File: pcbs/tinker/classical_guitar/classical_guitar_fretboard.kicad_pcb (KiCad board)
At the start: 4 copper layers, 188 parts, among them Q1 AO3401A, U1 AT42QT1110-A, U2 AT42QT1110-A, U3 AT42QT1110-A, U4 MP2359

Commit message: Prepare electrode tracking
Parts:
- removed Udecoder4_to_161: CD74HC154ME4, Package_SO:SOIC-24W_7.5x15.4mm_P1.27mm
- added Dec1: CD74HC4515M, Package_SO:SOIC-24W_7.5x15.4mm_P1.27mm, F.Cu at (43.2, 112.2)
- Jdecoder4_to_16_input1: value Conn_01x04_Male -> Conn_01x06_Male; footprint Connector_PinSocket_2.54mm:PinSocket_1x04_P2.54mm_Vertical -> Connector_PinHeader_2.54mm:PinHeader_1x06_P2.54mm_Vertical
- moved Jcommon_spi1 54.4 mm to (65.6, 81.1)
- moved Jdecoder4_to_16_output1 51.9 mm to (58.4, 131.3), turned to 180 degrees
- moved Jdecoder4_to_16_input1 49.5 mm to (30.5, 119.0), turned to 180 degrees
- moved Jch1 19.8 mm to (65.6, 69.8)
- moved Jsync1 19.8 mm to (65.6, 63.6)
- moved Rch1 19.8 mm to (58.8, 63.4)
- moved JPch1 19.8 mm to (60.0, 68.4)
- moved JPch2 19.8 mm to (60.0, 72.4)
- moved JPch3 19.8 mm to (60.0, 76.4)
- moved D1 6.27 mm to (58.8, 23.2)
- moved Jpower1 5.22 mm to (30.5, 38.1)
- moved Q1 3.71 mm to (54.0, 28.1)
- moved F1 3.48 mm to (60.6, 30.8)
- moved D2 0.40 mm to (53.2, 38.0)
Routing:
- net Net-(Dec1-Pad1): track 35.9 -> 7.69 mm
- net Net-(Dec1-Pad21): track 0.00 -> 21.7 mm
- net Net-(Dec1-Pad23): track 34.4 -> 13.5 mm
- net Net-(Dec1-Pad15): track 41.3 -> 23.0 mm
- net Net-(Dec1-Pad13): track 31.6 -> 14.8 mm
- net Net-(Dec1-Pad5): track 6.80 -> 22.5 mm
- net Net-(Dec1-Pad4): track 7.33 -> 23.0 mm
- net Net-(Dec1-Pad6): track 6.78 -> 22.4 mm
- net Net-(Dec1-Pad7): track 7.31 -> 22.4 mm
- net Net-(Dec1-Pad8): track 8.26 -> 21.9 mm
- net Net-(Dec1-Pad9): track 9.94 -> 23.5 mm, vias 0 -> 2
- net Net-(Dec1-Pad16): track 36.4 -> 23.4 mm, vias 0 -> 2
- net GND: track 0.00 -> 12.7 mm
- net VDD: track 0.00 -> 12.5 mm
- net /mp2359/BUCK_SW: track 0.00 -> 11.9 mm
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
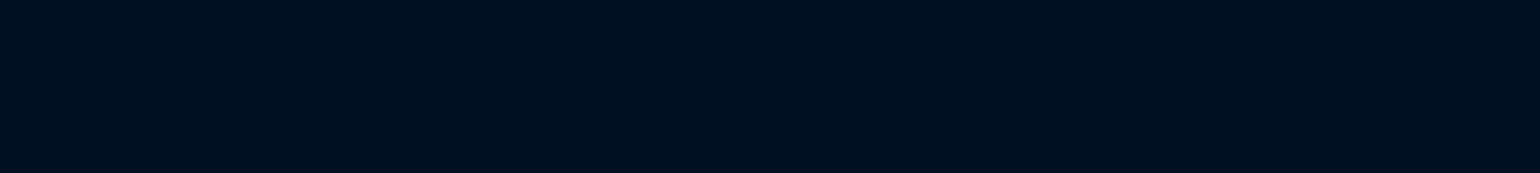
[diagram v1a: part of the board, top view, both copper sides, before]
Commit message: Adjusted last_move
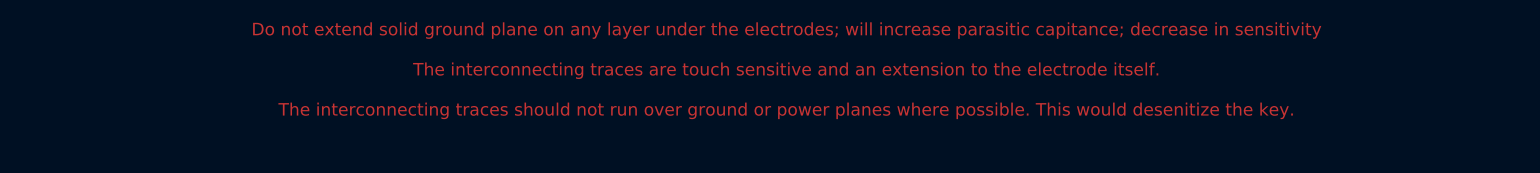
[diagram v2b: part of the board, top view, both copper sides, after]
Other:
- board text added: "Do not extend solid ground plane on any layer under the electrodes; will increase parasitic capitance; decrease in sensitivity The interconnecting traces are touch sensitive and an extension to the electrode itself. The interconnecting traces should not run over ground or power planes where possible. This would desenitize the key."
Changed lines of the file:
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@@
   (general
     (thickness 1.6)
-    (drawings 0)
+    (drawings 1)
     (tracks 742)
     (zones 0)
@@
     )
   )
+  (gr_text "Do not extend solid ground plane on any layer under the electrodes; will increase parasitic capitance; decrease in sensitivity\n\nThe interconnecting traces are touch sensitive and an extension to the electrode itself. \n\nThe interconnecting traces should not run over ground or power planes where possible. This would desenitize the key." (at 172.325 -24.35) (layer F.Cu)
+    (effects (font (size 1.5 1.5) (thickness 0.3)))
+  )
   (segment (start 85.6175 28.125) (end 85.525 28.0325) (width 0.3) (layer F.Cu) (net 1))

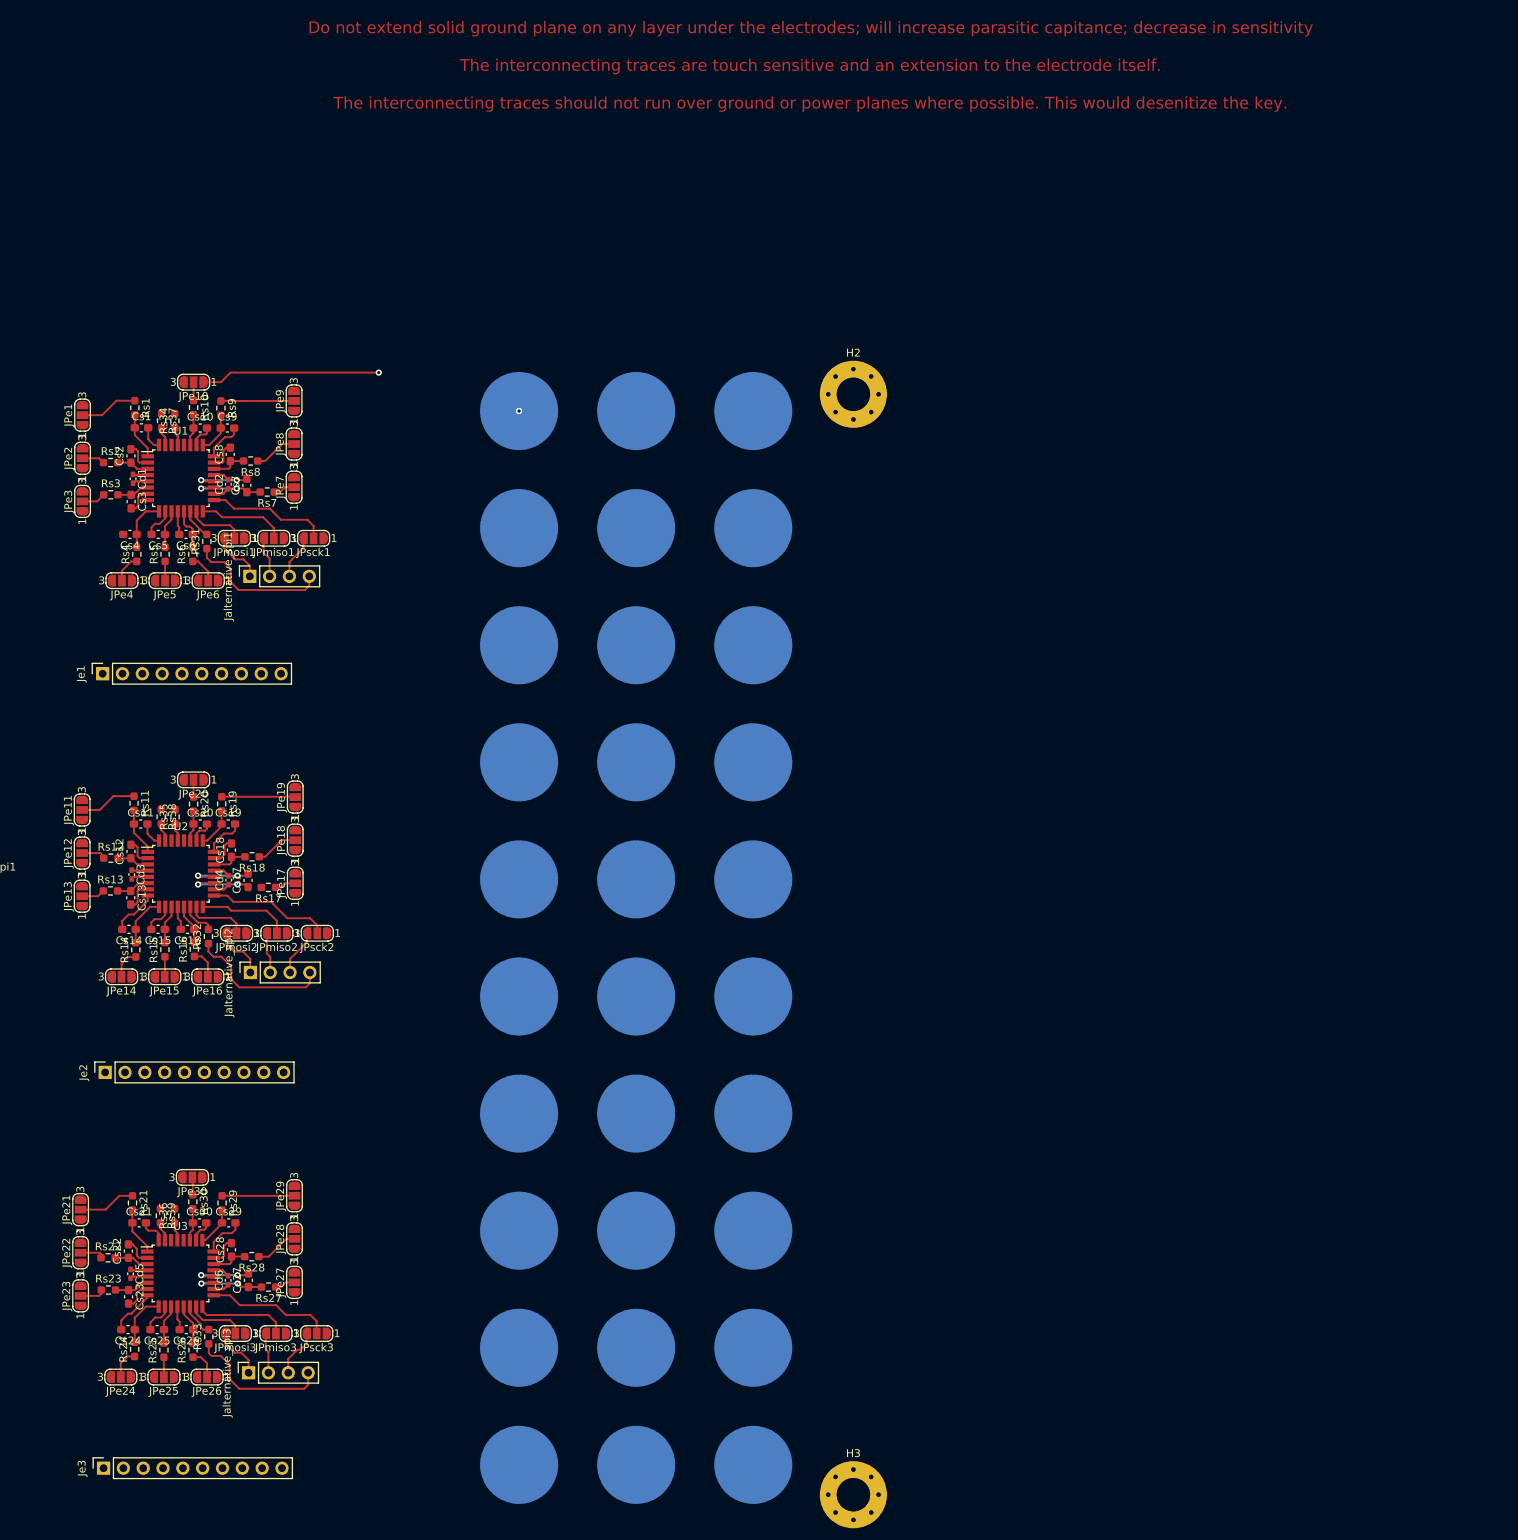
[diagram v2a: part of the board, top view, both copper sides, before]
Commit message: Tracing electrodes
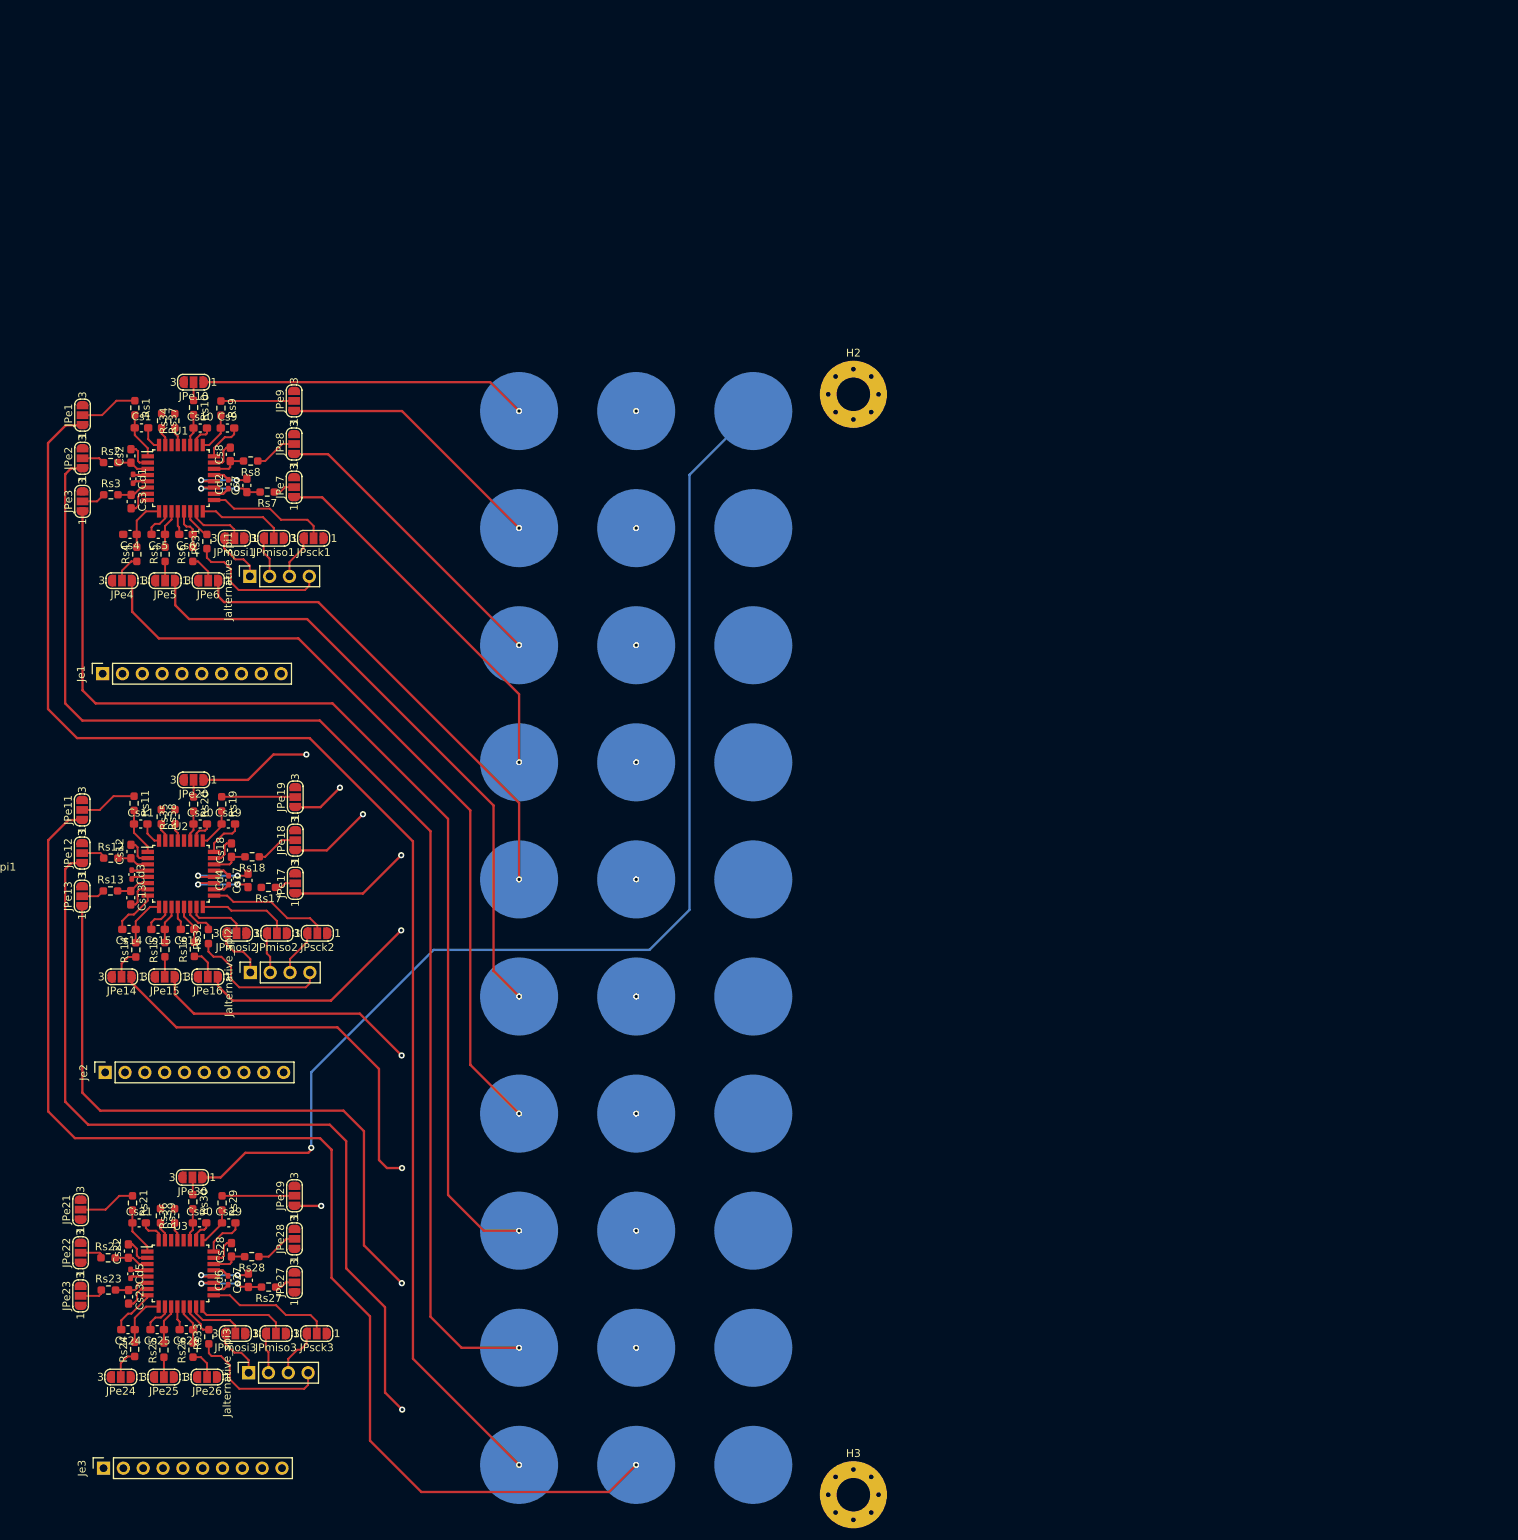
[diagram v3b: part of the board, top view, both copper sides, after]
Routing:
- net Net-(E1-Pad1): track 0.00 -> 178.7 mm, vias 0 -> 1
- net Net-(E2-Pad1): track 0.00 -> 160.7 mm, vias 0 -> 1
- net Net-(E11-Pad1): track 0.00 -> 156.1 mm, vias 0 -> 1
- net Net-(E30-Pad1): track 0.00 -> 149.7 mm, vias 0 -> 1
- net Net-(E12-Pad1): track 0.00 -> 141.0 mm, vias 0 -> 2
- net Net-(E3-Pad1): track 0.00 -> 135.7 mm, vias 0 -> 1
- net Net-(E13-Pad1): track 0.00 -> 116.3 mm, vias 0 -> 2
- net Net-(E4-Pad1): track 0.00 -> 99.3 mm, vias 0 -> 1
- net Net-(E14-Pad1): track 0.00 -> 84.9 mm, vias 0 -> 2
- net Net-(E20-Pad1): track 0.00 -> 82.1 mm, vias 0 -> 2
- net Net-(E5-Pad1): track 0.00 -> 80.4 mm, vias 0 -> 1
- net Net-(E15-Pad1): track 0.00 -> 67.7 mm, vias 0 -> 2
- net Net-(E16-Pad1): track 0.00 -> 62.0 mm, vias 0 -> 2
- net Net-(E6-Pad1): track 0.00 -> 61.3 mm, vias 0 -> 1
- net Net-(E19-Pad1): track 0.00 -> 58.9 mm, vias 0 -> 2
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
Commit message: Traced electrodes
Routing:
- net Net-(E29-Pad1): track 3.42 -> 152.4 mm, vias 1 -> 4
- net Net-(E21-Pad1): track 0.00 -> 130.9 mm, vias 0 -> 1
- net Net-(E28-Pad1): track 0.00 -> 130.2 mm, vias 0 -> 3
- net Net-(E22-Pad1): track 0.00 -> 129.7 mm, vias 0 -> 4
- net Net-(E26-Pad1): track 0.00 -> 127.0 mm, vias 0 -> 3
- net Net-(E27-Pad1): track 0.00 -> 125.2 mm, vias 0 -> 3
- net Net-(E23-Pad1): track 0.00 -> 121.8 mm, vias 0 -> 3
- net Net-(E25-Pad1): track 0.00 -> 120.0 mm, vias 0 -> 5
- net Net-(E24-Pad1): track 0.00 -> 118.4 mm, vias 0 -> 3
- net Net-(E30-Pad1): track 149.7 -> 165.7 mm, vias 1 -> 2
- net Net-(E1-Pad1): track 178.7 -> 185.2 mm
- net Net-(E11-Pad1): track 156.1 -> 157.8 mm

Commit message: Traced 1st at42qt1110
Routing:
- net Net-(Jsync1-Pad1): track 0.00 -> 168.4 mm, vias 0 -> 2
- net /C_MISO: track 0.00 -> 119.0 mm, vias 0 -> 6
- net /C_SCK: track 0.00 -> 115.7 mm, vias 0 -> 4
- net /C_MOSI: track 0.00 -> 102.5 mm, vias 0 -> 4
- net /Change1: track 0.00 -> 85.1 mm
- net Net-(JPe10-Pad3): track 0.00 -> 77.3 mm, vias 0 -> 12
- net /Change3: track 0.00 -> 68.8 mm
- net Net-(JPe9-Pad3): track 0.00 -> 62.6 mm, vias 0 -> 8
- net /Change2: track 0.00 -> 58.5 mm, vias 0 -> 6
- net Net-(JPe8-Pad3): track 0.00 -> 47.2 mm, vias 0 -> 6
- net Net-(JPe1-Pad3): track 0.00 -> 43.0 mm, vias 0 -> 3
- net Net-(JPe7-Pad3): track 0.00 -> 40.3 mm, vias 0 -> 4
- net Net-(JPe2-Pad3): track 0.00 -> 33.5 mm, vias 0 -> 2
- net Net-(JPe3-Pad3): track 0.00 -> 33.2 mm, vias 0 -> 2
- net Net-(JPe4-Pad3): track 0.00 -> 14.6 mm
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
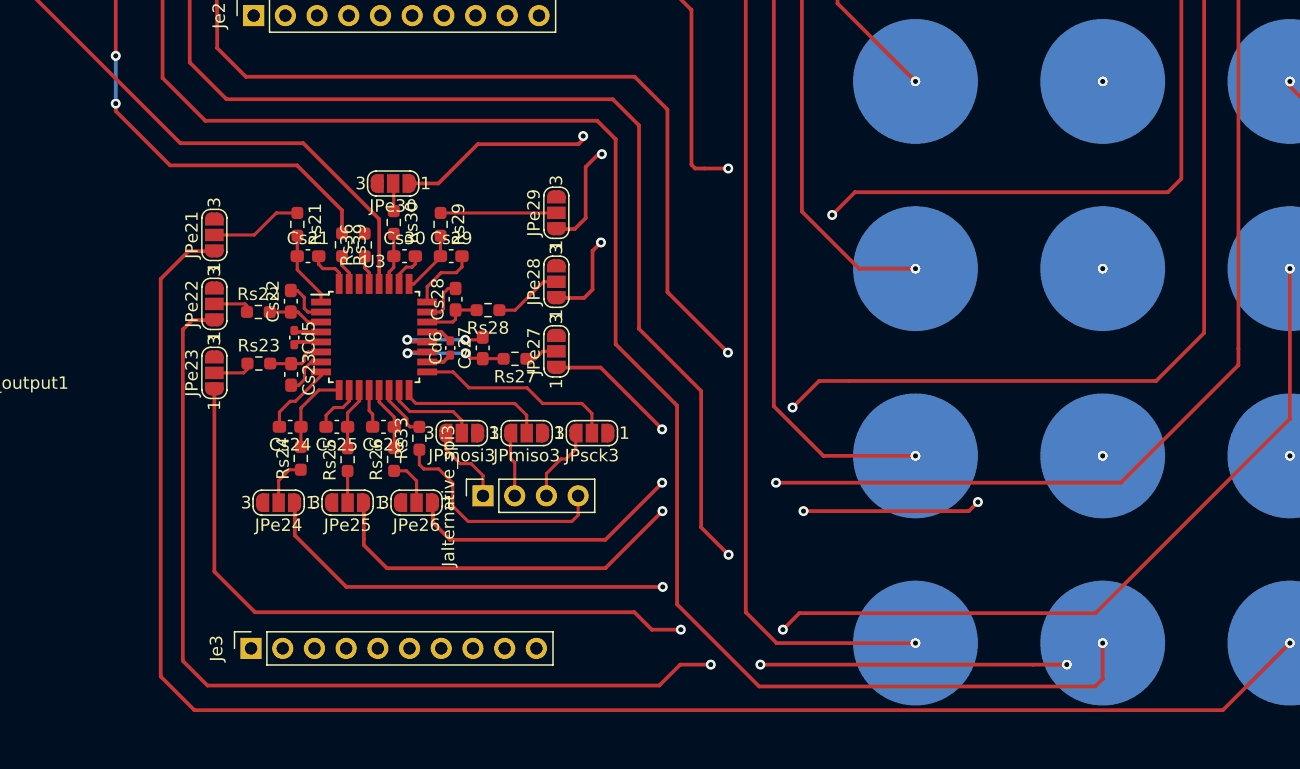
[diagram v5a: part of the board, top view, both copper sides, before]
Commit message: Traced 2nd at42qt1110
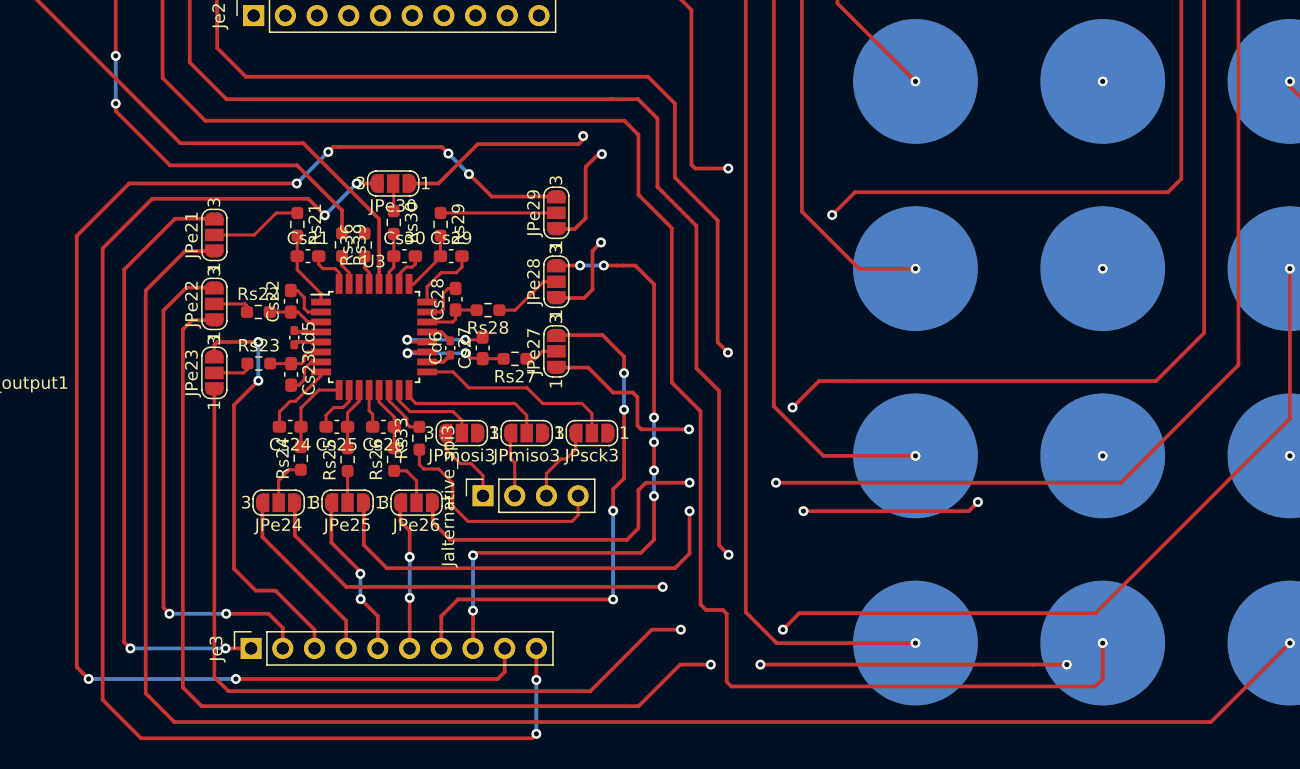
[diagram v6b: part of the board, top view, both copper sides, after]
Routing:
- net Net-(JPe29-Pad3): track 0.00 -> 114.4 mm, vias 0 -> 6
- net Net-(JPe30-Pad3): track 0.00 -> 104.4 mm, vias 0 -> 4
- net Net-(JPe28-Pad3): track 0.00 -> 51.4 mm, vias 0 -> 8
- net Net-(JPe21-Pad3): track 0.00 -> 49.1 mm, vias 0 -> 2
- net Net-(JPe27-Pad3): track 0.00 -> 42.9 mm, vias 0 -> 4
- net Net-(JPe22-Pad3): track 0.00 -> 40.5 mm, vias 0 -> 2
- net Net-(JPe23-Pad3): track 0.00 -> 33.5 mm, vias 0 -> 2
- net Net-(JPe24-Pad3): track 0.00 -> 14.5 mm
- net Net-(JPe25-Pad3): track 0.00 -> 13.2 mm, vias 0 -> 2
- net Net-(JPe26-Pad3): track 0.00 -> 12.0 mm, vias 0 -> 2
- net Net-(E23-Pad1): track 121.8 -> 130.8 mm
- net Net-(E21-Pad1): track 130.9 -> 134.3 mm
- net Net-(E11-Pad1): track 157.8 -> 161.1 mm
- net Net-(E22-Pad1): track 129.7 -> 132.3 mm
- net Net-(E25-Pad1): track 120.0 -> 122.0 mm
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
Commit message: Traced 2nd at42qt1110 2
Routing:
- net /C_MISO: track 119.0 -> 275.4 mm, vias 6 -> 16
- net /C_SCK: track 115.7 -> 218.0 mm, vias 4 -> 10
- net /C_MOSI: track 102.5 -> 203.4 mm, vias 4 -> 8
- net Net-(JPe14-Pad3): track 0.00 -> 15.1 mm
- net Net-(JPe15-Pad3): track 0.00 -> 13.9 mm, vias 0 -> 2
- net Net-(JPe16-Pad3): track 0.00 -> 12.6 mm, vias 0 -> 2

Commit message: Almost finalized pcb
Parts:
- moved H3 2.00 mm to (177.8, 160.8)
- moved H4 2.00 mm to (31.8, 160.8)
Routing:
- net Net-(JPe20-Pad3): track 0.00 -> 59.7 mm, vias 0 -> 12
- net Net-(JPe19-Pad3): track 0.00 -> 58.3 mm, vias 0 -> 12
- net Net-(JPe11-Pad3): track 0.00 -> 49.6 mm, vias 0 -> 2
- net /C_MOSI: track 203.4 -> 252.6 mm, vias 8 -> 12
- net Net-(JPe18-Pad3): track 0.00 -> 47.0 mm, vias 0 -> 8
- net Net-(JPe17-Pad3): track 0.00 -> 42.8 mm, vias 0 -> 4
- net Net-(JPe12-Pad3): track 0.00 -> 40.3 mm, vias 0 -> 2
- net Net-(JPe13-Pad3): track 0.00 -> 32.3 mm, vias 0 -> 2
- net Net-(E11-Pad1): track 161.1 -> 163.0 mm
- net Net-(Cs17-Pad1): track 8.66 -> 10.4 mm
- net Net-(E16-Pad1): track 62.0 -> 63.1 mm
- net /C_SCK: track 218.0 -> 216.8 mm
- net /Change2: track 58.5 -> 57.8 mm
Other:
- board outline added: 157.6 x 154.4 mm
